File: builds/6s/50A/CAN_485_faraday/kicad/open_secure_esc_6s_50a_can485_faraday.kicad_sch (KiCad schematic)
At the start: 66 parts, among them J1 J_SWD, J2 J_CAN, J3 J_RS485, J4A PH_A_TERM, J4B PH_B_TERM, J4C PH_C_TERM, J5A VM_TERM, J5B GND_TERM, Q1 TPHR8504PL, Q2 TPHR8504PL, Q3 TPHR8504PL, Q4 TPHR8504PL, Q5 TPHR8504PL, Q6 TPHR8504PL, U1 MSPM0G3518_Q1_PM, U2 OPTIGA_TRUST_M, U3 ADM3055E/ADM3057E, U4 ADM2582E/ADM2587E, U5 DRV8353S, U6 INA240, U7 INA240, U8 INA240

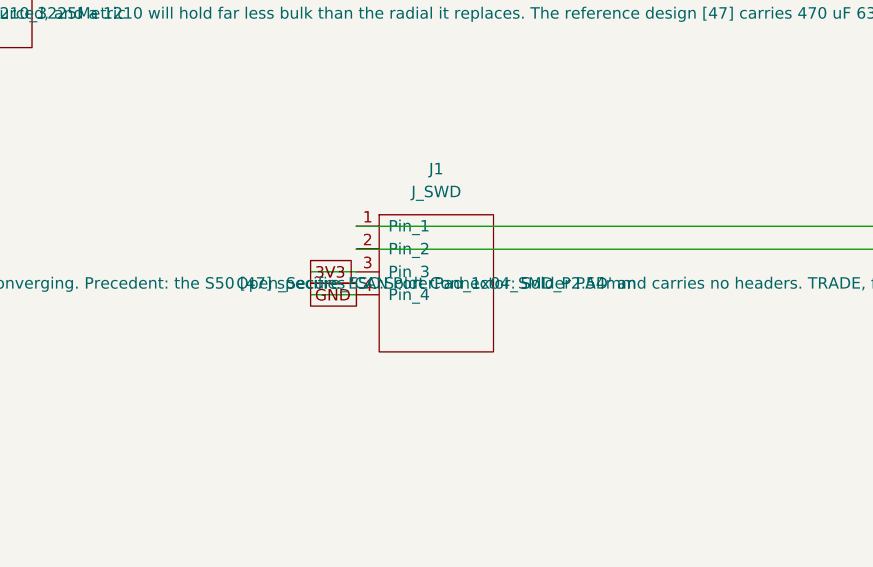
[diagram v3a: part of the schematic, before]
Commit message: Shrink J1 to a 1.27 mm probe pattern: 36.0 -> 12.0 mm2
J1 is the SWD debug port (SWDIO/SWCLK to U1.12/U1.13, plus 3V3 and GND). It
was using the same 2.54 mm wire-solder pads as J2/J3, which it does not need:
gen_smd_solder_pad_footprints.py already argued "For J1 (SWD) this is fine --
it is a bring-up/debug interface, not a flight connection."

    was  SolderPad_1x04_SMD_P2.54mm         9.22 x 3.20 mm, 36.0 mm2
    now  SolderPad_1x04_SMD_P1.27mm_Probe   4.71 x 1.80 mm, 12.0 mm2

1.27 mm is the pitch standard pogo-pin debug jigs use, so an off-the-shelf
4-pin inline fixture fits, and staying single-row keeps that fixture trivial.
A 2x2 grid would have saved a further ~2.5 mm2 but needs a custom one.
Pad-to-pad gap is 0.37 mm. Rejected: Tag-Connect TC2030, which looks like the
compact answer but needs three through-board alignment holes -- on a
double-sided board those cost their area twice, a net loss here.

The generator is now parameterised per variant rather than by module-level
constants, and carries a separate description template for probe pads so the
new footprint cannot be mistaken for a wire pad. J2/J3 deliberately KEEP the
2.54 mm variant: they leave the board in service and their solder area is
load-bearing in a way J1's is not (TODO.md 12.5.k). Verified that both
existing footprints regenerate byte-identical apart from uuids.

Footprint swapped in both the schematic and the PCB with all four nets
preserved. ERC 0 errors.

Not caused by this change, noted while checking: 2 copper_edge_clearance on
J5A/J5B against the board's rounded-corner arcs are present both before and
after, so they predate the swap.

Co-Authored-By: Claude Opus 5 <noreply@anthropic.com>
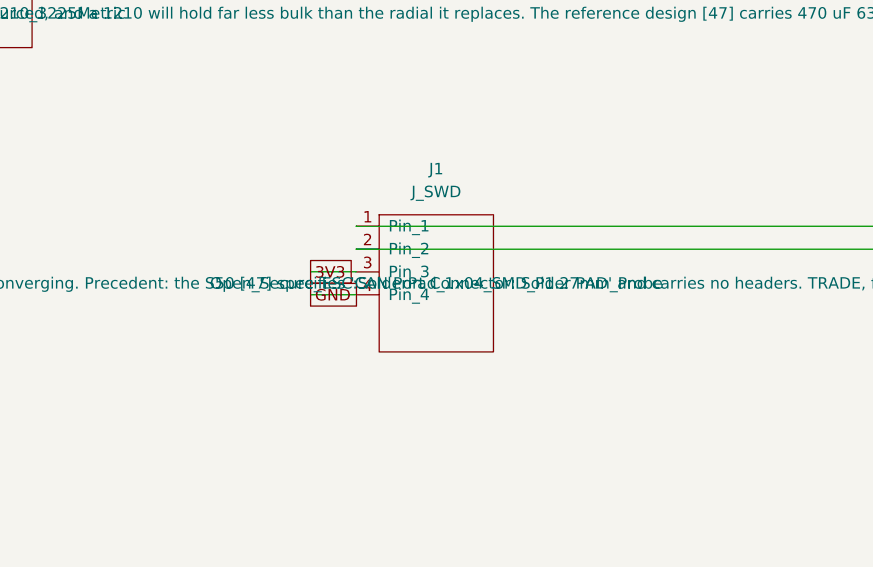
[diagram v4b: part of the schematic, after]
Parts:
- J1: footprint Open_Secure_ESC:SolderPad_1x04_SMD_P2.54mm -> Open_Secure_ESC:SolderPad_1x04_SMD_P1.27mm_Probe
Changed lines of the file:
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@@
   )
   (wire (pts (xy 509.85 196.19) (xy 509.85 191.10999999999999))
-    (stroke (width 0.0))
+    (stroke (width 0))
   )
   (wire (pts (xy 509.85 208.89) (xy 509.85 213.97))
-    (stroke (width 0.0))
+    (stroke (width 0))
   )
   (wire (pts (xy 509.85 226.19) (xy 509.85 221.10999999999999))
-    (stroke (width 0.0))
+    (stroke (width 0))
   )
   (wire (pts (xy 509.85 238.89) (xy 509.85 243.97))
-    (stroke (width 0.0))
+    (stroke (width 0))
   )
   (wire (pts (xy 509.85 256.19) (xy 509.85 251.11))
-    (stroke (width 0.0))
+    (stroke (width 0))
   )
   (wire (pts (xy 509.85 268.89000000000004) (xy 509.85 273.97))
-    (stroke (width 0.0))
+    (stroke (width 0))
   )
   (wire (pts (xy 509.85 286.19) (xy 509.85 281.11))
-    (stroke (width 0.0))
+    (stroke (width 0))
   )
   (wire (pts (xy 509.85 298.89000000000004) (xy 509.85 303.97))
-    (stroke (width 0.0))
+    (stroke (width 0))
   )
   (wire (pts (xy 509.85 416.19) (xy 509.85 411.11))
-    (stroke (width 0.0))
+    (stroke (width 0))
   )
   (wire (pts (xy 509.85 428.89000000000004) (xy 509.85 433.97))
-    (stroke (width 0.0))
+    (stroke (width 0))
   )
   (wire (pts (xy 509.85 446.19) (xy 509.85 441.11))
-    (stroke (width 0.0))
+    (stroke (width 0))
   )
   (wire (pts (xy 509.85 458.89000000000004) (xy 509.85 463.97))
-    (stroke (width 0.0))
+    (stroke (width 0))
   )
   (wire (pts (xy 509.85 476.19) (xy 509.85 471.11))
-    (stroke (width 0.0))
+    (stroke (width 0))
   )
   (wire (pts (xy 509.85 488.89000000000004) (xy 509.85 493.97))
-    (stroke (width 0.0))
+    (stroke (width 0))
   )
   (wire (pts (xy 509.85 506.18999999999994) (xy 509.85 501.10999999999996))
-    (stroke (width 0.0))
+    (stroke (width 0))
   )
   (wire (pts (xy 509.85 518.89) (xy 509.85 523.9699999999999))
-    (stroke (width 0.0))
+    (stroke (width 0))
   )
   (text "nFAULT: pulled up only, not wired to MCU in this build -- open item, see ../README.md"
@@
       (effects (font (size 1.27 1.27)))
     )
-    (property "Footprint" "Open_Secure_ESC:SolderPad_1x04_SMD_P2.54mm" (at 219.85 62.54 0)
-      (effects (font (size 1.27 1.27)))
-    )
+    (property "Footprint" "Open_Secure_ESC:SolderPad_1x04_SMD_P1.27mm_Probe" (at 219.85 62.54 0)
+      (effects (font (size 1.27 1.27)))
+    )

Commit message: Waterproof/thermal design doc, BOM creepage audit, RHB MCU package swap
Three related pieces of work on builds/6s/50A/CAN_485_faraday:

- docs/design-waterproofing-and-thermal-management.md: layered ingress
  protection for a faceted/hinged ESC (conformal coating + baffled vents
  + drainage + sealed wire egress), replacing the never-authored
  design-submersible-cooling.md placeholder README/TODO pointed at.
  Splits the IP requirement into a vented splash/spray variant (keeps
  the sibling repo's aspirated cooling path alive) and a sealed/immersion
  variant (needs a metal conduction path instead), since a single
  gasketed enclosure would silently defeat the cooling analysis already
  done for the nacelle case. Cites IEC 60529 and IPC-CC-830C from local
  verified copies (REFERENCES.md [56][57]).

- docs/solutions/architecture-patterns/: two new trap docs from a
  full creepage audit against a fixed 50A/6S working-voltage class.
  smaller-package-does-not-shrink-creepage.md shows a smaller isolator
  package (ISO1042 SOIC-8, ISOW1412) needs MORE creepage than the parts
  already in the BOM, because creepage tracks working voltage, not
  package size. bom-creepage-audit-can485-faraday.md ranks the real
  levers: MCU package is the biggest one, ADM3055E->ADM3057E is a free
  0.5mm (REFERENCES.md [10] addendum), and flags CAN/RS-485 barrier
  consolidation and PCB groove techniques as open research, not BOM
  items yet. New citations REFERENCES.md [59]-[61].

- MCU package swap PM (LQFP-64, ~10x10mm) -> RHB (VQFN-32, 5x5mm) for
  U1, same MSPM0G3518-Q1 die: cuts isolation_envelope.py's "widest
  non-isolated part" from 12.90mm toward ~6.5mm. symbols/
  MSPM0G3518_Q1_RHB.kicad_sym was a prior generic, unwired, character-
  named symbol built for an unrelated board; scrubbed and re-wired here
  with this build's own pin roles (verified conflict-free against [44]
  Fig 6-6 / Table 6-2), fixing a real defect found in the process (a
  spurious 33rd pin -- RHB is a 32-pin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
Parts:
- U1: value MSPM0G3518_Q1_PM -> MSPM0G3518_Q1_RHB; footprint Package_QFP:LQFP-64_10x10mm_P0.5mm -> Package_DFN_QFN:Texas_RHB0032E_VQFN-32-1EP_5x5mm_P0.5mm_EP3.45x3.45mm; symbol MSPM0G3518_Q1_PM:MSPM0G3518_Q1_PM -> MSPM0G3518_Q1_RHB:MSPM0G3518_Q1_RHB
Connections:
- net 3V3: now also U1.4 (VDD); no longer U1.40 (VDD)
- net ADC_IU: now also U1.28 (ADC_IU); no longer U1.25 (ADC_IU)
- net ADC_IV: now also U1.27 (ADC_IV); no longer U1.24 (ADC_IV)
- net ADC_IW: now also U1.29 (ADC_IW); no longer U1.26 (ADC_IW)
- net GD_SPI_MISO: now also U1.20 (GD_SPI_MISO); no longer U1.2 (GD_SPI_MISO)
- net GND: now also U1.5 (VSS); no longer U1.41 (VSS)
- net NRST: now also U1.3 (NRST); no longer U1.38 (NRST)
- net RS485_DE_RE: now also U1.10 (RS485_DE_RE); no longer U1.37 (RS485_DE_RE)
- net SE_I2C_SCL: now also U1.19 (SE_I2C_SCL); no longer U1.8 (SE_I2C_SCL)
- net SE_RST: now also U1.18 (SE_RST); no longer U1.7 (SE_RST)
- net VBUS_SENSE: now also U1.25 (ADC_VBUS); no longer U1.17 (ADC_VBUS)
- net at U1.1 (RS485_TXD): now also U4.7 (TxD); no longer U5.30 (nSCS)
- net at U1.12 (PWM_AH): now also U5.32 (INHA); no longer J1.1 (Pin_1)
- net at U1.13 (PWM_AL): now also U5.33 (INLA); no longer J1.2 (Pin_2)
- net at U5.28 (SDI): now also U1.22 (GD_SPI_MOSI); no longer U1.3 (GD_SPI_MOSI)
- net at U3.7 (TXD): now also U1.16 (CAN_TX); no longer U1.30 (CAN_TX)
- net at U3.5 (RXD): now also U1.17 (CAN_RX); no longer U1.31 (CAN_RX)
- net at U4.4 (RxD): now also U1.2 (RS485_RXD); no longer U1.34 (RS485_RXD)
- net at U5.29 (SCLK): now also U1.21 (GD_SPI_SCK); no longer U1.4 (GD_SPI_SCK)
- net at U5.36 (INHC): now also U1.14 (PWM_CH); no longer U1.47 (PWM_CH)
- net at U5.37 (INLC): now also U1.15 (PWM_CL); no longer U1.48 (PWM_CL)
- net at U5.34 (INHB): now also U1.7 (PWM_BH); no longer U1.52 (PWM_BH)
- net at U5.35 (INLB): now also U1.8 (PWM_BL); no longer U1.53 (PWM_BL)
- new net: J1.1 (Pin_1), U1.23 (SWDIO)
- new net: J1.2 (Pin_2), U1.24 (SWCLK)
- new net: U1.6 (GD_SPI_CS), U5.30 (nSCS)
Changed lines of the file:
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@@
     )
   )
-  (symbol (lib_id "MSPM0G3518_Q1_PM:MSPM0G3518_Q1_PM") (at 529.85 292.54 0) (unit 1)
+  (symbol (lib_id "MSPM0G3518_Q1_RHB:MSPM0G3518_Q1_RHB") (at 529.85 292.54 0) (unit 1)
     (in_bom yes) (on_board yes) (dnp no)
     (property "Reference" "U1" (at 529.85 276.03 0)
       (effects (font (size 1.27 1.27)))
     )
-    (property "Value" "MSPM0G3518_Q1_PM" (at 529.85 278.57 0)
+    (property "Value" "MSPM0G3518_Q1_RHB" (at 529.85 278.57 0)
       (effects (font (size 1.27 1.27)))
     )
-    (property "Footprint" "Package_QFP:LQFP-64_10x10mm_P0.5mm" (at 529.85 292.54 0)
+    (property "Footprint" "Package_DFN_QFN:Texas_RHB0032E_VQFN-32-1EP_5x5mm_P0.5mm_EP3.45x3.45mm" (at 529.85 292.54 0)
       (effects (font (size 1.27 1.27)))
     )
@@
       (effects (font (size 1.27 1.27)))
     )
-    (property "Description" "TI MSPM0G3518-Q1 Arm Cortex-M0+ MCU, PM (LQFP-64, 12x12mm) package, orderable M0G3518QPMRQ1 -- project MCU as of 2026-08-10, replacing the NXP S32K144 (REFERENCES.md [31], superseded). Swapped in for its AES-128/256 accelerator with GCM support plus a hardware keystore, which lifts the AES-128 ceiling the S32K144's SHE-compliant CSEc imposed (finding C-01 in docs/secure-element-architecture.md). The Infineon OPTIGA(TM) Trust M secure element (REFERENCES.md [45], schematic U2) is UNAFFECTED by this swap and remains required: the MSPM0's AES engine is symmetric-only, so the Trust M still provides asymmetric PKI device authentication (ECDSA over a fab-provisioned key + X.509 certificate) and ephemeral session-key agreement (ECDHE + KDF), while the MCU consumes the agreed session key for the per-frame authenticated hot path. See docs/secure-element-architecture.md for the full division of labour." (at 529.85 292.54 0)
+    (property "Description" "TI MSPM0G3518-Q1 Arm Cortex-M0+ MCU, RHB (VQFN-32, 5x5mm body) package, orderable M0G3518QRHBRQ1 -- swapped 2026-09-06 from the PM (LQFP-64) package (REFERENCES.md [44], same die/part number) to shrink docs/tools/isolation_envelope.py's 'widest non-isolated part' per docs/solutions/architecture-patterns/bom-creepage-audit-can485-faraday.md finding #1. AES-128/256 + GCM accelerator and hardware keystore unaffected by the package change (finding C-01 in docs/secure-element-architecture.md). The Infineon OPTIGA(TM) Trust M secure element (REFERENCES.md [45], schematic U2) remains required and unaffected: the MSPM0's AES engine is symmetric-only, so the Trust M still provides asymmetric PKI device authentication and ephemeral session-key agreement, while the MCU consumes the agreed session key for the per-frame authenticated hot path. See docs/secure-element-architecture.md for the full division of labour." (at 529.85 292.54 0)
       (effects (font (size 1.27 1.27)))
     )
